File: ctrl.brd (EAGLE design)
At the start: 58 x 58 mm, 47 parts, among them U1 TPS92513, U2 TPS92513

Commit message: save
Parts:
- removed D10, D11, D12, D13, D14, D3, D4, D5, D6, D7: XPGWHT-L1-0000-00BE8, derek:XLAMP-XPG
- removed J45: (no value), derek:1X07_NO_SILK
- added U$1, U$2: 10M, derek:0402
- added U$10, U$3, U$4, U$5, U$7, U$8, U$9: TP-1502, derek:TP-1502
- added U$6: 10k, derek:0603
- added U3: ESP-WROOM-32, derek:ESP-WROOM-32
- moved C2 30.9 mm to (13.4, 25.5)
- moved C4 30.9 mm to (3.04, 22.2)
- moved C5 30.9 mm to (4.91, 19.9)
- moved C6 30.9 mm to (10.2, 21.5)
- moved C7 30.9 mm to (8.23, 16.1)
- moved C8 30.9 mm to (16.4, 12.9)
- moved D2 30.9 mm to (11.0, 17.6)
- moved L1 30.9 mm to (15.6, 18.4)
- moved R2 30.9 mm to (6.84, 26.4)
- moved R3 30.9 mm to (3.54, 23.6)
- moved R4 30.9 mm to (5.11, 22.9)
- moved R5 30.9 mm to (7.04, 14.3)
- moved C1 30.9 mm to (11.3, 25.5)
- moved C3 30.9 mm to (9.25, 24.8)
- moved D1 30.9 mm to (17.1, 25.3)
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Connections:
- removed net N$12: D6.C, D7.A
- removed net N$13: D3.C, D4.A
- removed net N$14: D4.C, D5.A
- removed net N$15: D5.C, D6.A
- removed net N$2: D11.C, D12.A
- removed net N$22: D13.C, D14.A
- removed net N$24: D10.A, D14.C
- removed net N$27: D10.C, D11.A
- new net 3.3V: U$3.1, U$6.2, U3.2
- new net N$29: U$6.1, U3.3
- net 24V: now also U$1.2, U$2.2, U$4.1; no longer J45.7
- net CLK: now also U3.10; no longer J45.1
- net GND-ISO: now also U$10.1, U3.1, U3.15, U3.38, U3.GND; no longer D10.GND, D10.P$1, D10.P$2, D10.P$3, D11.GND, D11.P$1, D11.P$2, D11.P$3, D12.GND, D12.P$1, D12.P$2, D12.P$3, D13.GND, D13.P$1, D13.P$2, D13.P$3, D14.GND, D14.P$1, D14.P$2, D14.P$3, D3.GND, D3.P$1, D3.P$2, D3.P$3, D4.GND, D4.P$1, D4.P$2, D4.P$3, D5.GND, D5.P$1, D5.P$2, D5.P$3, D6.GND, D6.P$1, D6.P$2, D6.P$3, D7.GND, D7.P$1, D7.P$2, D7.P$3, J45.6
- net IADJ1: now also U$1.1; no longer J45.5
- net IADJ2: now also U$2.1; no longer J45.2
- net N$23: now also U$8.1; no longer D12.C
- net N$26: now also U$9.1; no longer D13.A
- net N$6: now also U$7.1; no longer D3.A
- net N$7: now also U$5.1; no longer D7.C
- net PDIM1: now also U3.11; no longer J45.4
- net PDIM2: now also U3.12; no longer J45.3
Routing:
- net 24V: track 57.0 -> 3.63 mm, vias 1 -> 0
- net N$24: track 35.2 -> 0.00 mm
- net N$12: track 34.3 -> 0.00 mm
- net N$27: track 34.2 -> 0.00 mm
- net N$7: track 34.1 -> 0.00 mm
- net CLK: track 32.3 -> 0.00 mm
- net N$2: track 31.5 -> 0.00 mm
- net N$22: track 30.8 -> 0.00 mm
- net N$26: track 30.2 -> 0.00 mm
- net N$6: track 30.1 -> 0.00 mm
- net N$14: track 29.5 -> 0.00 mm, vias 2 -> 0
- net N$15: track 29.5 -> 0.00 mm
- net N$13: track 28.6 -> 0.00 mm
- net PDIM1: track 23.5 -> 0.00 mm, vias 1 -> 0
- net IADJ2: track 20.3 -> 1.74 mm, vias 1 -> 0
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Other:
- board size 58 x 58 mm -> 73.5 x 38 mm

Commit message: saveeee
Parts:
- removed U$10, U$3, U$4, U$5, U$7, U$8, U$9: TP-1502, derek:TP-1502
- added 24V, 3.3V, C+, C-, GND, W+, W-: TP-1502, derek:TP-1502
- moved U$6 36.7 mm to (41.0, 5.80)
- moved U3 26.7 mm to (35.1, 17.3), flipped to the bottom
- moved C2 8.73 mm to (16.4, 17.3)
- moved C3 8.73 mm to (12.3, 16.6)
- moved R4 8.73 mm to (8.11, 14.7)
- moved U1 8.73 mm to (10.6, 13.0)
- moved C1 8.73 mm to (14.3, 17.3)
- moved C4 8.73 mm to (6.04, 14.0)
- moved C5 8.73 mm to (7.91, 11.7)
- moved C6 8.73 mm to (13.2, 13.3)
- moved C7 8.73 mm to (11.2, 7.95)
- moved C8 8.73 mm to (19.4, 4.67)
- moved D1 8.73 mm to (20.1, 17.1)
- moved D2 8.73 mm to (14.0, 9.37)
- moved L1 8.73 mm to (18.6, 10.2)
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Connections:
- net 24V: now also 24V.1; no longer U$4.1
- net 3.3V: now also 3.3V.1; no longer U$3.1
- net GND-ISO: now also GND.1; no longer U$10.1
- net N$23: now also W+.1; no longer U$8.1
- net N$26: now also W-.1; no longer U$9.1
- net N$6: now also C-.1; no longer U$7.1
- net N$7: now also C+.1; no longer U$5.1
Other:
- board size 73.5 x 38 mm -> 52 x 34.9 mm

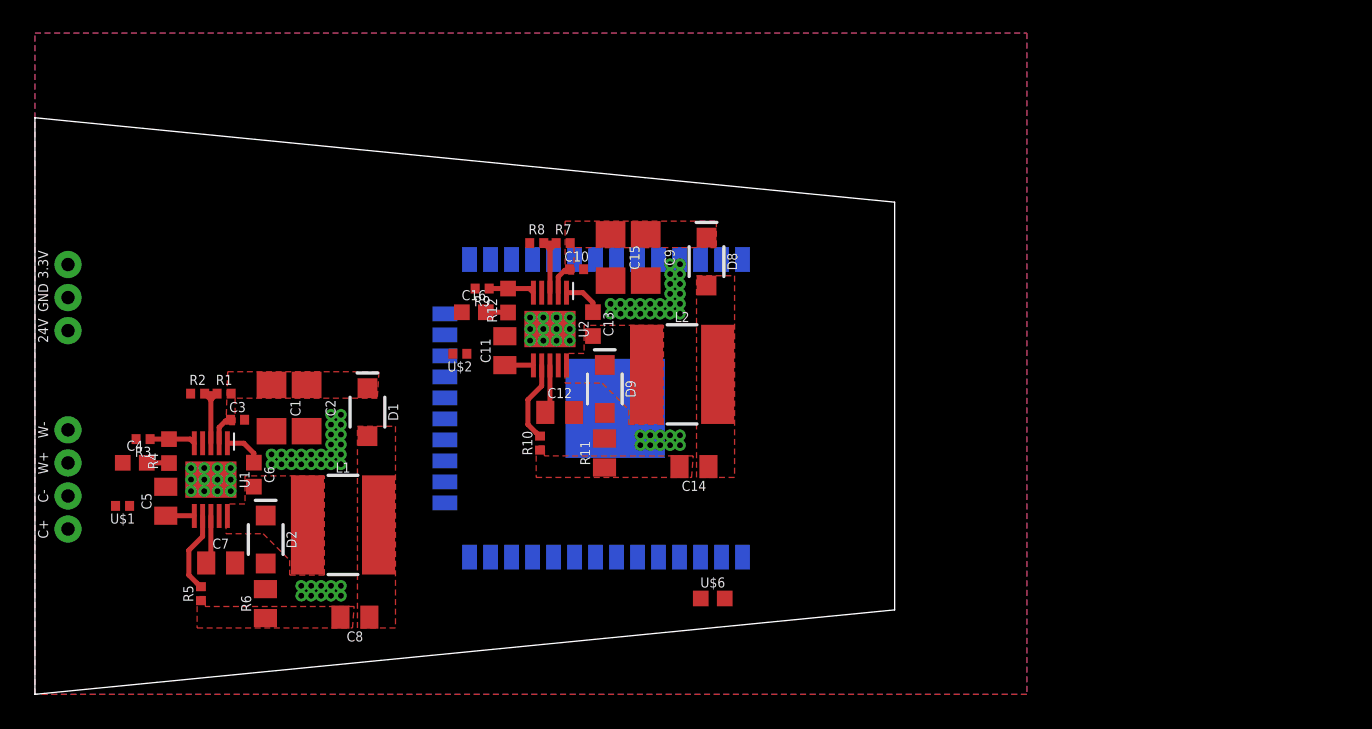
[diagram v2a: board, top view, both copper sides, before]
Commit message: rearrange positions
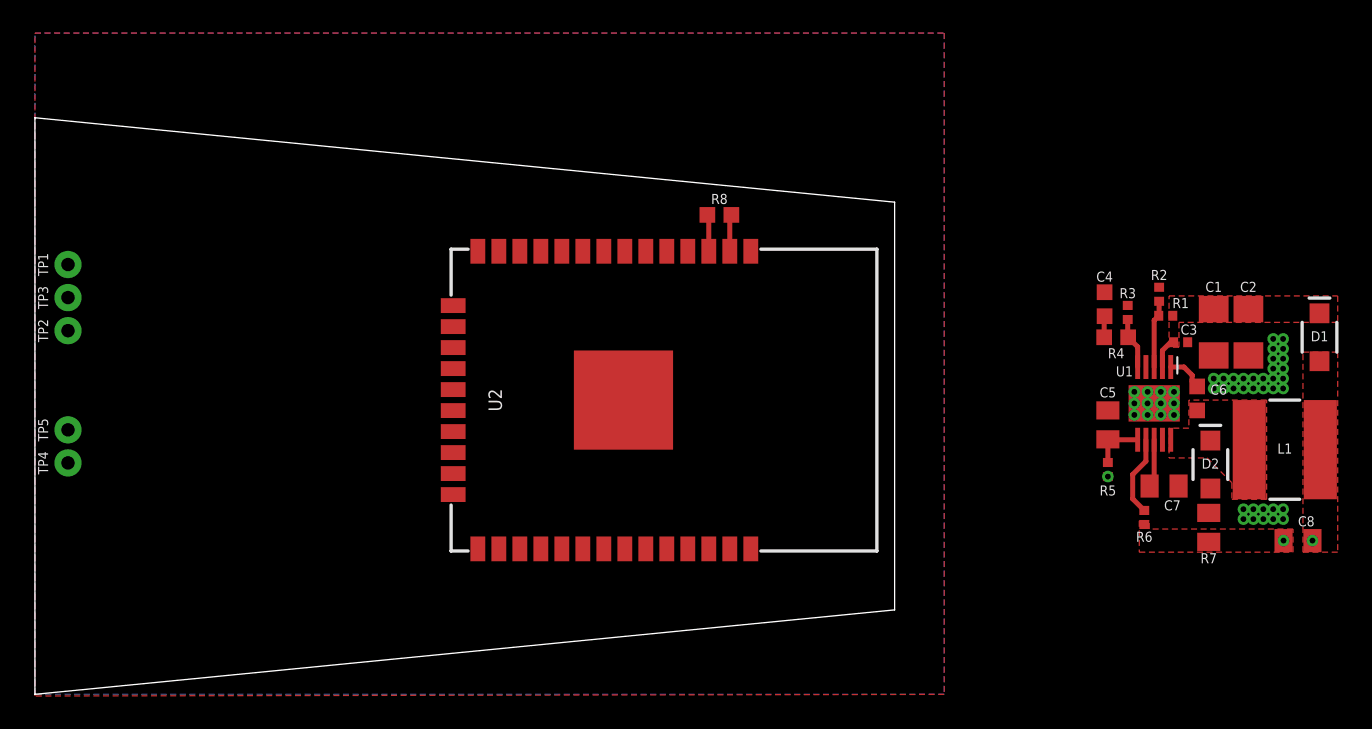
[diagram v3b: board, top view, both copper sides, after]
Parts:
- removed C+, C-: TP-1502, derek:TP-1502
- removed C10: 10000pF, derek:0402
- removed C11: 0.01μF, derek:0805
- removed C12: 0.1µF, derek:0805
- removed C13: 0.1µF, derek:0603
- removed C14: 1µF, derek:0805
- removed C15, C9: 1µF, derek:1206
- removed C16: 470pF, derek:0603
- removed D8, D9: PMEG6010CEH,115, derek:SOD-123F
- removed L2: 33µH, derek:SRN6045
- removed R10: 976, derek:0402
- removed R11: 0.51, derek:0805
- removed R12: 4.02k, derek:0603
- removed R9: 162k, derek:0402
- removed U$1, U$2: 10M, derek:0402
- removed U$6: 10k, derek:0603
- removed U3: ESP-WROOM-32, derek:ESP-WROOM-32
- R5: value 976 -> 10M
- R6: value 0.51 -> 976; device derek:0805 -> derek:0402
- R7: value 97.6k -> 0.51; device derek:0402 -> derek:0805
- R8: value 5.49k -> 10k; device derek:0402 -> derek:0603
- U2: value TPS92513 -> ESP-WROOM-32; device derek:TPS92513 -> derek:ESP-WROOM-32
- moved R3 60.0 mm to (66.1, 23.1), turned to 90 degrees
- moved C4 59.4 mm to (64.7, 23.6), turned to 90 degrees
- moved R2 58.5 mm to (68.0, 24.2), turned to 90 degrees
- moved D1 57.8 mm to (77.7, 21.6)
- moved R4 57.7 mm to (65.4, 21.6), turned to 0 degrees
- moved D2 57.3 mm to (71.1, 13.9)
- moved C7 57.3 mm to (68.3, 12.6)
- moved C6 57.2 mm to (70.3, 17.9)
- moved U1 57.2 mm to (67.7, 17.6)
- moved C3 57.2 mm to (69.3, 21.3)
- moved C8 57.2 mm to (76.4, 9.30)
- moved C1 57.2 mm to (71.3, 21.9)
- moved C5 57.2 mm to (64.9, 16.3)
- moved R1 57.2 mm to (68.4, 22.9)
- moved C2 57.2 mm to (73.4, 21.9)
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- renumbered 24V to TP2, 3.3V to TP1, GND to TP3, W+ to TP4, W- to TP5
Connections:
- removed net IADJ1: C5.1, U$1.1, U1.6
- removed net N$1 (its old number): R7.2, R8.1, U2.3
- removed net N$11: R5.2, U1.7
- removed net N$16 (its old number): C13.1, D9.C, L2.1, U2.10
- removed net N$17 (its old number): R12.2, R9.1, U2.5
- removed net N$18 (its old number): C12.1, U2.8
- removed net N$19 (its old number): C13.2, U2.1
- removed net N$25 (its old number): C16.1, R12.1
- removed net N$6: C-.1, C8.2, R5.1, R6.1
- removed net N$7: C+.1, C8.1, D1.A, L1.2
- net 24V: now also R5.2; no longer C10.1, C15.1, C9.1, D8.C, R7.1, U$1.2, U$2.2, U2.2
- net 3.3V: now also R8.2, U2.2; no longer U$6.2, U3.2
- net CLK: now also U2.10; no longer C16.2, U3.10
- net GND-ISO: now also R7.2, U2.1, U2.15, U2.38, U2.GND; no longer C10.2, C11.2, C12.2, C15.2, C9.2, D9.A, R11.2, R6.2, R8.2, R9.2, U2.9, U2.GND-ISO, U2.P$1, U2.P$10, U2.P$11, U2.P$12, U2.P$2, U2.P$3, U2.P$4, U2.P$5, U2.P$6, U2.P$7, U2.P$8, U2.P$9, U3.1, U3.15, U3.38, U3.GND
- net IADJ2: now also C5.1, R5.1, U1.6; no longer C11.1, U$2.1, U2.6
- net N$20: now also R6.2, U1.7; no longer R10.2, U2.7
- net N$23: now also C8.1, D1.A, L1.2; no longer C14.1, D8.A, L2.2
- net N$26: now also C8.2, R6.1, R7.1; no longer C14.2, R10.1, R11.1
- net N$29: now also R8.1, U2.3; no longer U$6.1, U3.3
- net PDIM1: now also U2.11; no longer U1.4, U3.11
- net PDIM2: now also U1.4, U2.12; no longer U2.4, U3.12
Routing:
- net N$11: track 4.94 -> 0.00 mm
- net N$1 (its old number): track 4.44 -> 0.00 mm
- net N$18 (its old number): track 3.11 -> 0.00 mm
- net N$17 (its old number): track 2.78 -> 0.00 mm
- net N$19 (its old number): track 2.42 -> 0.00 mm
- net 3.3V: track 0.00 -> 2.24 mm
- net N$29: track 0.00 -> 2.24 mm
- net 24V: track 3.63 -> 1.88 mm, vias 0 -> 1
- net IADJ1: track 1.74 -> 0.00 mm
- net IADJ2: track 1.74 -> 3.21 mm
- net N$25 (its old number): track 1.35 -> 0.00 mm
- removed copper zone on layer 1, net N$16 (its old number)
- removed copper zone on layer 1, net N$6
- removed copper zone on layer 1, net N$7

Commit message: save
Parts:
- removed TP1, TP2, TP3: TP-1502, derek:TP-1502
- added 24V, 3.3V, GND, W+, W-: TP-1502, derek:TP-1502
- added C10, C9: 1µF, derek:1206
- added C11: 10000pF, derek:0402
- added C12: 470pF, derek:0603
- added C13: 0.01μF, derek:0805
- added C14: 0.1µF, derek:0603
- added C15: 0.1µF, derek:0805
- added C16: 1µF, derek:0805
- added D3, D4: PMEG6010CEH,115, derek:SOD-123F
- added L2: 33µH, derek:SRN6045
- added R10: 162k, derek:0402
- added R11: 4.02k, derek:0603
- added R12: 10M, derek:0402
- added R13: 976, derek:0402
- added R14: 0.51, derek:0805
- added R15: 10k, derek:0603
- added R9: 5.49k, derek:0402
- added U3: ESP-WROOM-32, derek:ESP-WROOM-32
- R8: value 10k -> 97.6k; device derek:0603 -> derek:0402
- U2: value ESP-WROOM-32 -> TPS92513; device derek:ESP-WROOM-32 -> derek:TPS92513
- moved C2 56.7 mm to (16.7, 24.1)
- moved C4 56.7 mm to (8.00, 25.8)
- moved C5 56.7 mm to (8.20, 18.5)
- moved C8 56.7 mm to (19.7, 11.5)
- moved D1 56.7 mm to (21.0, 23.8)
- moved R1 56.7 mm to (11.7, 25.1)
- moved R2 56.7 mm to (11.3, 26.4)
- moved R4 56.7 mm to (8.70, 23.8)
- moved R5 56.7 mm to (8.20, 15.8)
- moved R7 56.7 mm to (14.3, 12.3)
- moved U1 56.7 mm to (11.0, 19.8)
- moved C1 56.7 mm to (14.6, 24.1)
- moved C3 56.7 mm to (12.6, 23.5)
- moved C6 56.7 mm to (13.6, 20.1)
- moved C7 56.7 mm to (11.6, 14.8)
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- renumbered TP4 to C+, TP5 to C-
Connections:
- new net IADJ1: C13.1, R12.1, U2.6
- new net N$10: C-.1, C16.2, R13.1, R14.1
- new net N$2: R8.2, R9.1, U2.3
- new net N$3: C14.1, D4.C, L2.1, U2.10
- new net N$4: R10.1, R11.2, U2.5
- new net N$5: C15.1, U2.8
- new net N$6: C14.2, U2.1
- new net N$7: R13.2, U2.7
- new net N$8: C12.1, R11.1
- new net N$9: C+.1, C16.1, D3.A, L2.2
- net 24V: now also 24V.1, C10.1, C11.1, C9.1, D3.C, R12.2, R8.1, U2.2; no longer TP2.1
- net 3.3V: now also 3.3V.1, R15.2, U3.2; no longer R8.2, TP1.1, U2.2
- net CLK: now also C12.2, U3.10; no longer U2.10
- net GND-ISO: now also C10.2, C11.2, C13.2, C15.2, C9.2, D4.A, GND.1, R10.2, R14.2, R9.2, U2.9, U2.GND-ISO, U2.P$1, U2.P$10, U2.P$11, U2.P$12, U2.P$2, U2.P$3, U2.P$4, U2.P$5, U2.P$6, U2.P$7, U2.P$8, U2.P$9, U3.1, U3.15, U3.38, U3.GND; no longer TP3.1, U2.1, U2.15, U2.38, U2.GND
- net N$23: now also W+.1; no longer C+.1
- net N$26: now also W-.1; no longer C-.1
- net N$29: now also R15.1, U3.3; no longer R8.1, U2.3
- net PDIM1: now also U2.4, U3.11; no longer U2.11
- net PDIM2: now also U3.12; no longer U2.12
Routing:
- net 24V: track 1.88 -> 81.0 mm, vias 1 -> 0
- net CLK: track 0.04 -> 65.6 mm, vias 0 -> 2
- net 3.3V: track 2.24 -> 58.2 mm
- net PDIM2: track 0.00 -> 44.2 mm, vias 0 -> 1
- net N$9: track 0.00 -> 43.4 mm
- net N$10: track 0.00 -> 42.4 mm
- net N$23: track 0.00 -> 25.3 mm, vias 1 -> 0
- net N$26: track 0.00 -> 25.0 mm, vias 1 -> 0
- net PDIM1: track 0.00 -> 23.8 mm, vias 0 -> 1
- net N$7: track 0.00 -> 4.90 mm
- net N$2: track 0.00 -> 4.10 mm
- net IADJ1: track 0.00 -> 3.21 mm
- net N$4: track 0.00 -> 3.12 mm
- net N$5: track 0.00 -> 2.91 mm
- net N$6: track 0.00 -> 2.31 mm
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- added copper zone on layer 1, net N$10
- added copper zone on layer 1, net N$3
- added copper zone on layer 1, net N$9
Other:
- board size 52 x 34.9 mm -> 70.3 x 86 mm

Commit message: ORDERED
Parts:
- moved C1 2.24 mm to (12.6, 25.1)
- moved C10 2.24 mm to (34.7, 25.1)
- moved C11 2.24 mm to (30.6, 24.5)
- moved C12 2.24 mm to (26.0, 26.8)
- moved C13 2.24 mm to (26.2, 19.5)
- moved C14 2.24 mm to (31.6, 21.1)
- moved C15 2.24 mm to (29.6, 15.8)
- moved C16 2.24 mm to (37.7, 12.5)
- moved C2 2.24 mm to (14.7, 25.1)
- moved C3 2.24 mm to (10.6, 24.5)
- moved C4 2.24 mm to (6.00, 26.8)
- moved C6 2.24 mm to (11.6, 21.1)
- moved C7 2.24 mm to (9.60, 15.8)
- moved C8 2.24 mm to (17.7, 12.5)
- moved C9 2.24 mm to (32.6, 25.1)
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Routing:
- net 24V: track 81.0 -> 66.3 mm, vias 0 -> 4
- net N$9: track 43.4 -> 41.2 mm
- net N$26: track 25.0 -> 23.1 mm
- net N$10: track 42.4 -> 40.7 mm
- net N$23: track 25.3 -> 23.7 mm
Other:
- board size 70.3 x 86 mm -> 50 x 36 mm
